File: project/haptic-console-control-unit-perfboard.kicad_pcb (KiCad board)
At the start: 2 copper layers, 90 x 144 mm, 31 parts, among them J1 JST-XH-5, J2 JST-XH-5

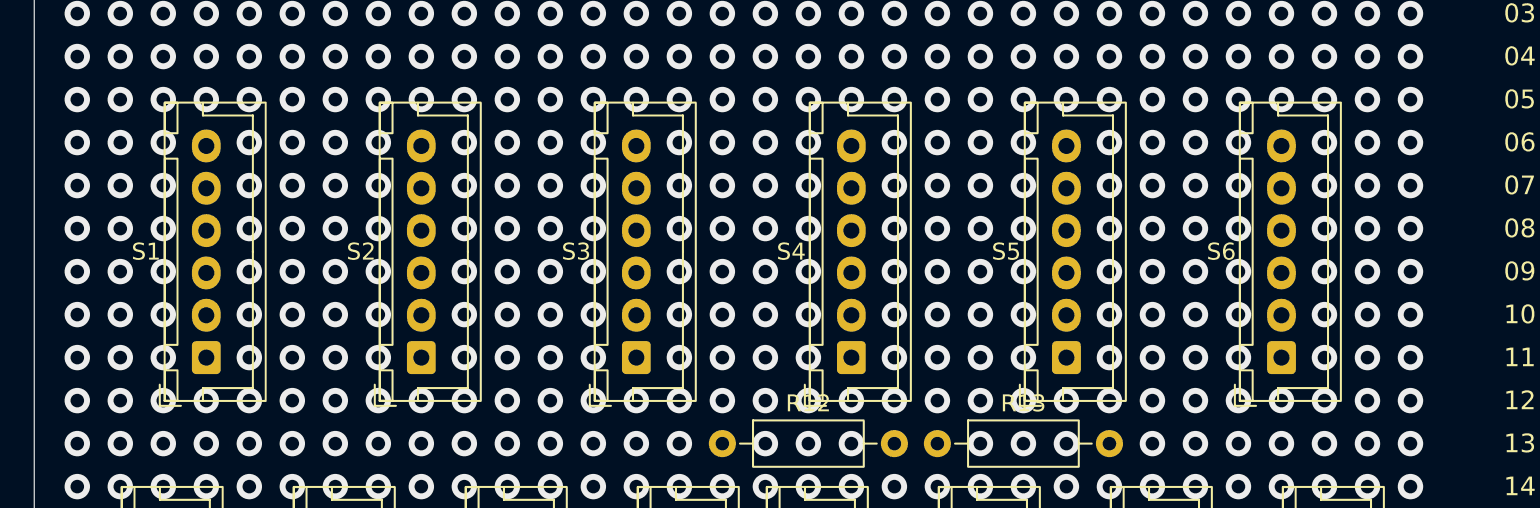
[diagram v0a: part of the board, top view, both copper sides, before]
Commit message: Add TP1-TP5 test points (SDA/SCL/GND/+3V3/+5V) to schematic and both boards
Schematic: 5 TestPoint symbols wired near the R12/R13 pullup network.
Manufactured board: 5 THT test pads routed around the existing autorouted
copper. Perfboard: real male 2.54mm header pins (not flat pads) at the
board's last column, with S1-S6 shifted one column left to clear them.
Wiring guide and README updated to match; full session notes in CLAUDE.md.

Co-Authored-By: Claude Sonnet 5 <noreply@anthropic.com>
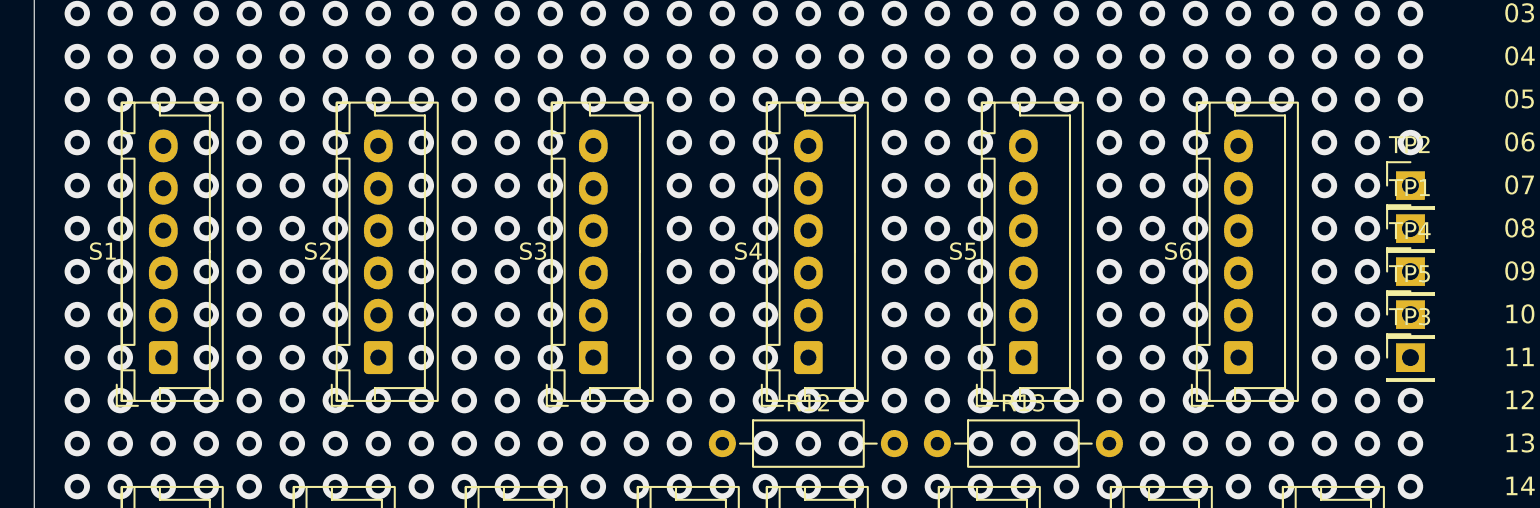
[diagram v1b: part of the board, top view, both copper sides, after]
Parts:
- added TP1: TP_SDA, Connector_PinHeader_2.54mm:PinHeader_1x01_P2.54mm_Vertical, F.Cu at (81.3, 20.3)
- added TP2: TP_SCL, Connector_PinHeader_2.54mm:PinHeader_1x01_P2.54mm_Vertical, F.Cu at (81.3, 17.8)
- added TP3: TP_GND, Connector_PinHeader_2.54mm:PinHeader_1x01_P2.54mm_Vertical, F.Cu at (81.3, 27.9)
- added TP4: TP_5V, Connector_PinHeader_2.54mm:PinHeader_1x01_P2.54mm_Vertical, F.Cu at (81.3, 22.9)
- added TP5: TP_3V3, Connector_PinHeader_2.54mm:PinHeader_1x01_P2.54mm_Vertical, F.Cu at (81.3, 25.4)
- moved S1 2.54 mm to (7.62, 27.9)
- moved S2 2.54 mm to (20.3, 27.9)
- moved S3 2.54 mm to (33.0, 27.9)
- moved S4 2.54 mm to (45.7, 27.9)
- moved S5 2.54 mm to (58.4, 27.9)
- moved S6 2.54 mm to (71.1, 27.9)
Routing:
- net (no net): vias 1496 -> 1467
